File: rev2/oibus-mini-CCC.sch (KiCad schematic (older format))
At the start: 88 parts, among them J1 Conn_01x04_Female, J2 USB_B_Micro, J3 uavcan_5pins, J4 Conn_01x02_Female, P1 TC2030-MCP, Q1 DMG3415U-7, Q2 NMOS, Q3 NMOS, SW1 SW_Push, U1 AP2112K-3.3, U10 TPD3E001DRLR, U2 SAM-M8Q, U3 NINA-B311-00B, U4 MCP73831-2-OT, U5 MCP1624T, U6 SHT31-DIS-B, U7 TCAN330, U8 STM32F303CCTx, U9 DW01C-G, Y1 16M, Y2 32kHz

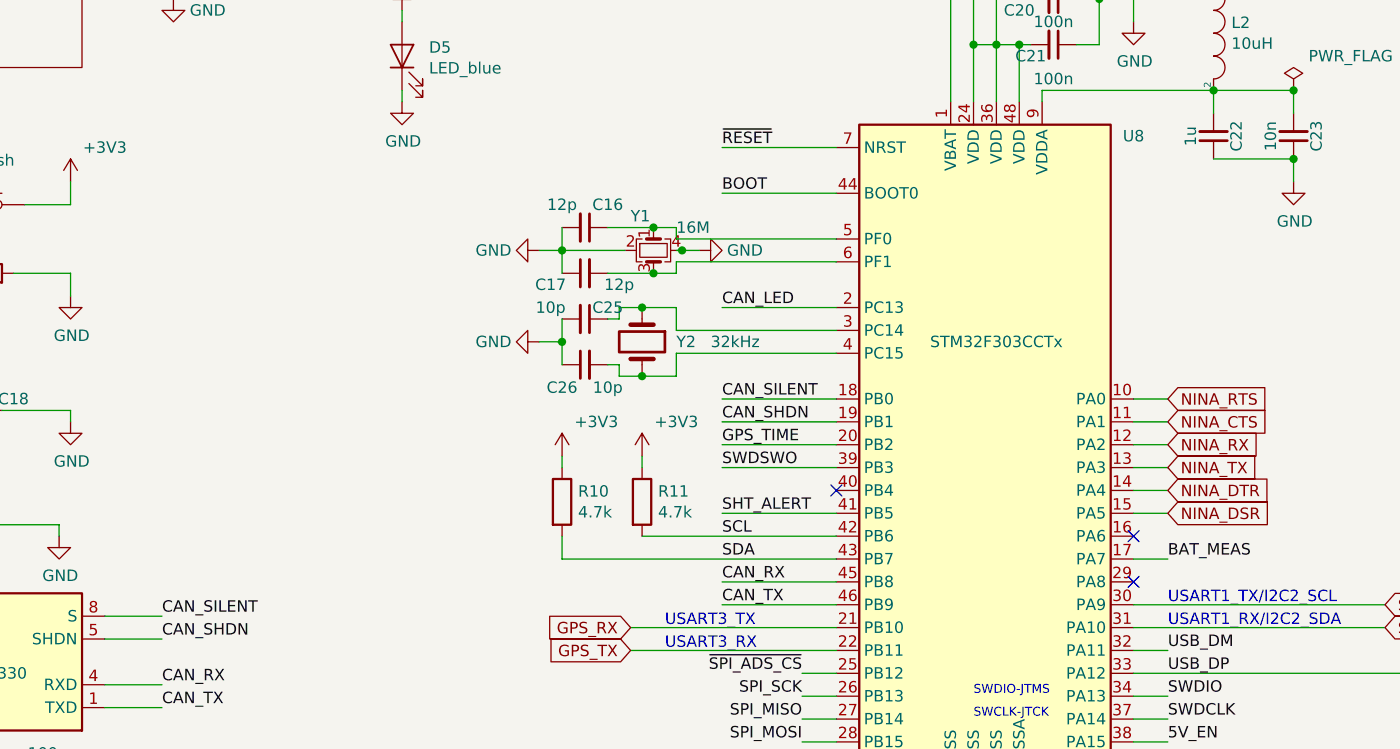
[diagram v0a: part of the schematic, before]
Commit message: added cut-out for SHT sensor, rotated battery connector, added on-off button
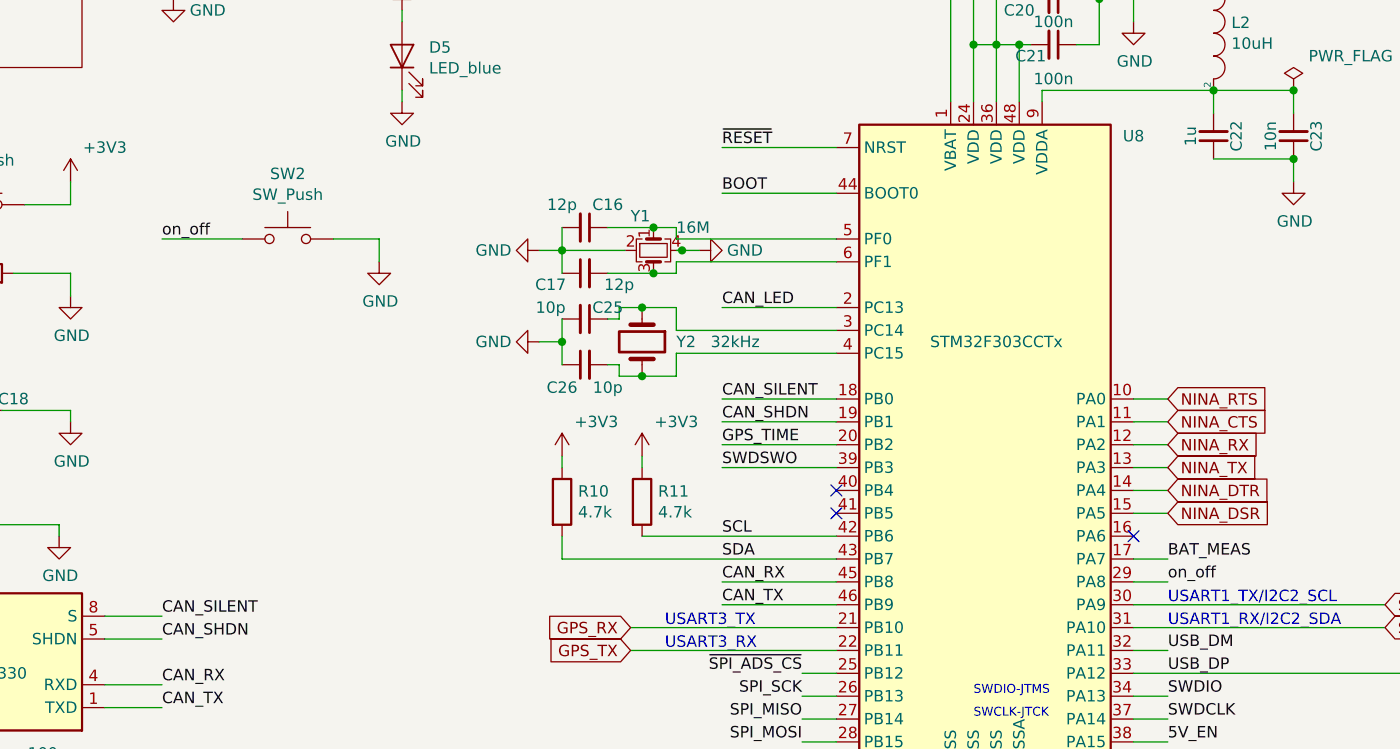
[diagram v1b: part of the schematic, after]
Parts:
- added SW2: SW_Push, Button_Switch_SMD:SW_SPST_EVQP7C, symbol Switch:SW_Push
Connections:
- net GND: now also SW2.2
- net SHT_ALERT: no longer U8.41 (PB5)
- net on_off: now reaches U8.29 (PA8)
- net on_off: now also SW2.1
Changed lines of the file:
@@
 Wire Wire Line
 	6550 3600 6350 3600
-Text Label 12150 3600 0    50   ~ 0
-SHT_ALERT
 Text Label 14100 3800 0    50   ~ 0
 BAT_MEAS
@@
 Wire Wire Line
 	15050 4100 13950 4100
-Wire Wire Line
-	12150 3600 12650 3600
-NoConn ~ 13950 3900
 NoConn ~ 1450 5000
 NoConn ~ 1450 5100
@@
 	11700 3000 11800 3000
 Connection ~ 11800 3000
+$Comp
+L Switch:SW_Push SW2
+U 1 1 5DDAFB3F
+P 10250 2400
+F 0 "SW2" H 10250 2685 50  0000 C CNN
+F 1 "SW_Push" H 10250 2594 50  0000 C CNN
+F 2 "Button_Switch_SMD:SW_SPST_EVQP7C" H 10250 2600 50  0001 C CNN
+F 3 "~" H 10250 2600 50  0001 C CNN
+	1    10250 2400
+	1    0    0    -1
+$EndComp
+Wire Wire Line
+	13950 3900 14100 3900
+NoConn ~ 12650 3600
+Text Label 14100 3900 0    50   ~ 0
+on_off
+Text Label 9700 2400 0    50   ~ 0
+on_off
+Wire Wire Line
+	9700 2400 10050 2400
+Wire Wire Line
+	10450 2400 10650 2400
+Wire Wire Line
+	10650 2400 10650 2500
+$Comp
+L power:GND #PWR0107
+U 1 1 5DEF9452
+P 10650 2500
+F 0 "#PWR0107" H 10650 2250 50  0001 C CNN
+F 1 "GND" H 10655 2327 50  0000 C CNN
+F 2 "" H 10650 2500 50  0001 C CNN
+F 3 "" H 10650 2500 50  0001 C CNN
+	1    10650 2500
+	1    0    0    -1
+$EndComp
 $EndSCHEMATC
